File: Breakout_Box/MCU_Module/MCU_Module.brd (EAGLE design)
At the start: 40 x 26.1 mm, 18 parts, among them Q1 QUARZ5, U1 MIC5205-3.3, U2 MSP430G2553RHB32

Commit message: Licenses
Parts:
- renumbered SV3 to H1
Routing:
- net VCC: track 23.3 -> 15.4 mm, vias 2 -> 0
- net TEST: track 27.6 -> 23.0 mm, vias 3 -> 2
- net !RST: track 32.9 -> 28.3 mm, vias 3 -> 2
- net DVCC(3.3V): track 31.9 -> 27.3 mm, vias 3 -> 2
- net GND: track 72.7 -> 68.1 mm, vias 7 -> 4
- net P2.3: track 17.2 -> 13.2 mm, vias 1 -> 0
- net P2.5: track 11.8 -> 7.83 mm, vias 1 -> 0
- net P3.7: track 11.5 -> 7.56 mm, vias 1 -> 0
- net P3.6: track 10.7 -> 6.71 mm, vias 1 -> 0
- net P3.5: track 10.9 -> 6.93 mm, vias 1 -> 0
- net P3.4: track 19.0 -> 15.0 mm, vias 1 -> 0
- net P2.7: track 37.6 -> 33.7 mm, vias 3 -> 2
- net P2.4: track 14.0 -> 10.1 mm, vias 1 -> 0
- net P1.7: track 14.8 -> 10.9 mm, vias 1 -> 0
- net P1.6: track 12.4 -> 8.40 mm, vias 1 -> 0
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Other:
- board size 40 x 26.1 mm -> 38 x 24.1 mm
- board text added: "H1"
- board text removed: "C1"
- board text removed: "C2"
- board text removed: "C3"
- board text removed: "C4"
- board text removed: "C5"
- board text removed: "C6"
- board text removed: "C7"
- board text removed: "C8"
- board text removed: "LSEL"
- board text removed: "R1"
- board text removed: "U1"
- board text removed: "U2"

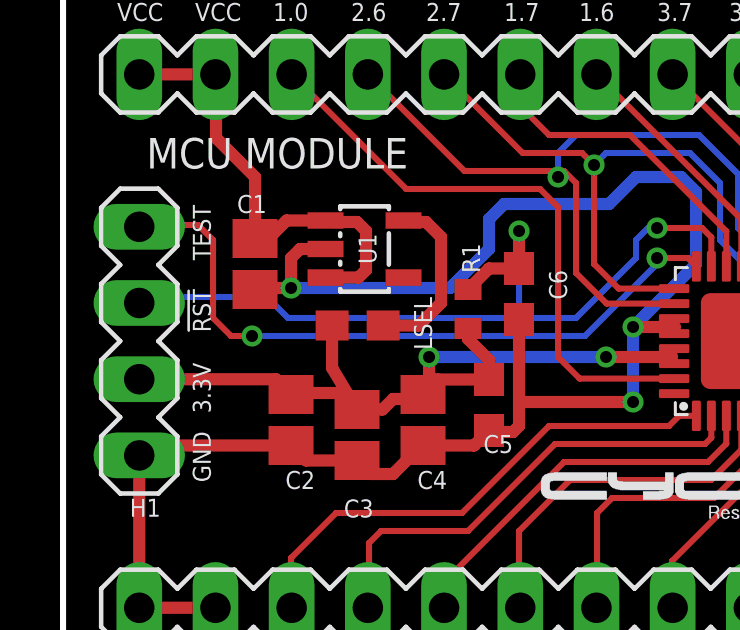
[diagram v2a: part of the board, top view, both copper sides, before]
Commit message: Slight Changes to MIDI and MCU: - Change BJT Part number on MIDI_Module - Delete Ferrite Bead on MCU_Module
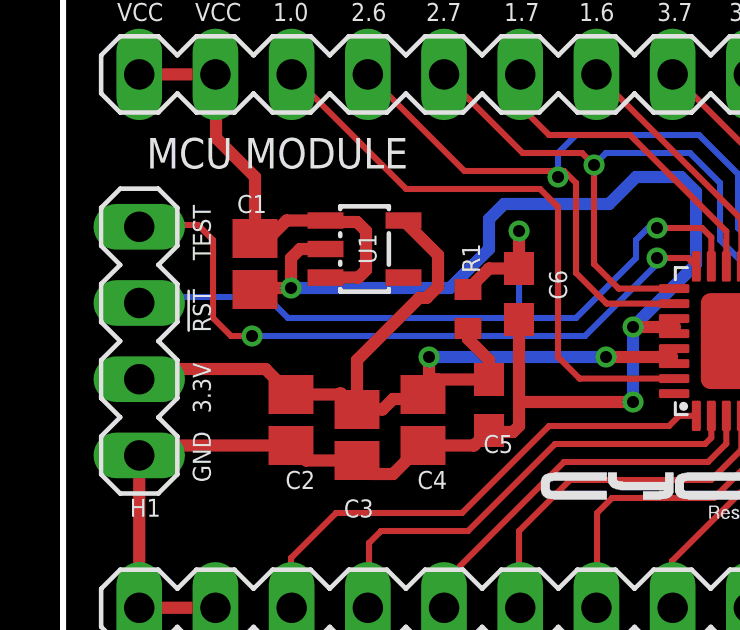
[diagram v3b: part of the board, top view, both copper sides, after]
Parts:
- removed LSEL: (no value), Cycfi:0603
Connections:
- removed net N$1: LSEL.1, U1.5
- net DVCC(3.3V): now also U1.5; no longer LSEL.2
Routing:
- net N$1: track 5.90 -> 0.00 mm
- net DVCC(3.3V): track 27.3 -> 32.7 mm
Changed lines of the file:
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@@
 <param name="mtIsolate" value="1.6mm 1.2mm 0.2mm 0.15mm 0.2mm 0.15mm 0.2mm 0.15mm 0.2mm 0.15mm 0.2mm 0.15mm 0.2mm 0.15mm 0.2mm"/>
 <param name="mdWireWire" value="6mil"/>
-<param name="mdWirePad" value="8mil"/>
+<param name="mdWirePad" value="6mil"/>
 <param name="mdWireVia" value="6mil"/>
-<param name="mdPadPad" value="12mil"/>
-<param name="mdPadVia" value="8mil"/>
-<param name="mdViaVia" value="12mil"/>
+<param name="mdPadPad" value="6mil"/>
+<param name="mdPadVia" value="6mil"/>
+<param name="mdViaVia" value="8mil"/>
 <param name="mdSmdPad" value="0mil"/>
 <param name="mdSmdVia" value="0mil"/>
@@
 <attribute name="VALUE" x="15.532" y="11.865" size="0.6" layer="27" ratio="14" rot="R90"/>
 </element>
-<element name="LSEL" library="Cycfi" package="0603" value="" x="9.82" y="11.95" smashed="yes" rot="R180">
-<attribute name="NAME" x="11.7" y="12.9" size="0.6" layer="25" ratio="14" rot="R270"/>
-<attribute name="VALUE" x="10.709" y="13.982" size="1.27" layer="27" rot="R180"/>
-</element>
 <element name="C6" library="resistor" package="C0603" value="1nf" x="15.2" y="13" smashed="yes" rot="R270">
 <attribute name="NAME" x="16.2" y="13.8" size="0.6" layer="25" ratio="14" rot="R270"/>
@@
 <wire x1="7.6" y1="13.2" x2="7.6" y2="14.2" width="0.4064" layer="1"/>
 <wire x1="7.6" y1="14.2" x2="7.9" y2="14.5" width="0.4064" layer="1"/>
-<wire x1="21.1" y1="14" x2="29.9" y2="13.6" width="0" layer="19" extent="16-16"/>
 </signal>
 <signal name="DVCC(3.3V)">
@@
 <contactref element="C5" pad="1"/>
 <contactref element="C3" pad="1"/>
-<contactref element="LSEL" pad="2"/>
-<contactref element="C2" pad="1"/>
 <contactref element="H1" pad="3"/>
-<wire x1="7.65" y1="9.7" x2="7.6" y2="9.65" width="0.4064" layer="1"/>
 <wire x1="14.2" y1="10.15" x2="12.5" y2="10.15" width="0.4064" layer="1"/>
 <wire x1="12.5" y1="10.15" x2="12.425" y2="10.075" width="0.4064" layer="1"/>
@@
 <wire x1="13.5" y1="11.5" x2="14.2" y2="10.8" width="0.4064" layer="1"/>
 <wire x1="14.2" y1="10.8" x2="14.2" y2="10.15" width="0.4064" layer="1"/>
-<wire x1="8.97" y1="11.95" x2="8.97" y2="10.53" width="0.4064" layer="1"/>
-<wire x1="8.97" y1="10.53" x2="9.8" y2="9.15" width="0.4064" layer="1"/>
-<wire x1="2.54" y1="10.16" x2="7.09" y2="10.16" width="0.4064" layer="1"/>
-<wire x1="7.09" y1="10.16" x2="7.6" y2="9.65" width="0.4064" layer="1"/>
 <wire x1="20.3695" y1="10.68" x2="20.3695" y2="11.18" width="0.2032" layer="1"/>
 <wire x1="20.3695" y1="10.68" x2="20.3695" y2="10.8305" width="0.2032" layer="1"/>
@@
 <wire x1="12.2" y1="10.9" x2="12.2" y2="10.3" width="0.4064" layer="1"/>
 <wire x1="12.2" y1="10.3" x2="12.425" y2="10.075" width="0.4064" layer="1"/>
-<wire x1="7.65" y1="9.7" x2="9.25" y2="9.7" width="0.4064" layer="1"/>
-<wire x1="9.25" y1="9.7" x2="9.8" y2="9.15" width="0.4064" layer="1"/>
+<wire x1="9.25" y1="9.7" x2="9.3" y2="9.65" width="0.4064" layer="1"/>
+<wire x1="9.475" y1="9.475" x2="9.8" y2="9.15" width="0.4064" layer="1"/>
 <wire x1="9.8" y1="9.15" x2="10.65" y2="9.15" width="0.4064" layer="1"/>
 <wire x1="10.65" y1="9.15" x2="11" y2="9.5" width="0.4064" layer="1"/>
 <wire x1="11" y1="9.5" x2="11.85" y2="9.5" width="0.4064" layer="1"/>
 <wire x1="11.85" y1="9.5" x2="12" y2="9.65" width="0.4064" layer="1"/>
+<contactref element="U1" pad="5"/>
+<contactref element="C2" pad="1"/>
+<wire x1="11.3501" y1="15.45" x2="12.5" y2="14.3001" width="0.4064" layer="1"/>
+<wire x1="12.1184375" y1="12.8686" x2="11.8686" y2="12.8686" width="0.4064" layer="1"/>
+<wire x1="12.5" y1="13.2501625" x2="12.1184375" y2="12.8686" width="0.4064" layer="1"/>
+<wire x1="12.5" y1="14.3001" x2="12.5" y2="13.2501625" width="0.4064" layer="1"/>
+<wire x1="9.8" y1="10.8" x2="9.8" y2="9.15" width="0.4064" layer="1"/>
+<wire x1="11.8686" y1="12.8686" x2="9.8" y2="10.8" width="0.4064" layer="1"/>
+<wire x1="7.6" y1="9.65" x2="7.51" y2="9.65" width="0.4064" layer="1"/>
+<wire x1="7.6" y1="9.65" x2="6.75" y2="10.5" width="0.4064" layer="1"/>
+<wire x1="2.88" y1="10.5" x2="2.54" y2="10.16" width="0.4064" layer="1"/>
+<wire x1="6.75" y1="10.5" x2="2.88" y2="10.5" width="0.4064" layer="1"/>
+<wire x1="7.6" y1="9.65" x2="9.3" y2="9.65" width="0.4064" layer="1"/>
+<wire x1="9.3" y1="9.65" x2="9.475" y2="9.475" width="0.4064" layer="1"/>
 </signal>
 <signal name="VCC">
@@
 <wire x1="6.55" y1="15" x2="6.4" y2="14.85" width="0.4064" layer="1"/>
 </signal>
-<signal name="N$1">
-<contactref element="U1" pad="5"/>
-<contactref element="LSEL" pad="1"/>
-<wire x1="10.67" y1="11.95" x2="11.85" y2="11.95" width="0.4064" layer="1"/>
-<wire x1="11.85" y1="11.95" x2="12.6" y2="12.7" width="0.4064" layer="1"/>
-<wire x1="12.6" y1="12.7" x2="12.6" y2="14.9" width="0.4064" layer="1"/>
-<wire x1="12.6" y1="14.9" x2="12.1" y2="15.4" width="0.4064" layer="1"/>
-<wire x1="12.1" y1="15.4" x2="11.6501" y2="15.4" width="0.4064" layer="1"/>
-<wire x1="11.6501" y1="15.4" x2="11.3501" y2="15.45" width="0.4064" layer="1"/>
-</signal>
 <signal name="P2.6">
